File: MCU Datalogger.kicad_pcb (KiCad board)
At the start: 2 copper layers, 32 parts, among them J1 Conn_01x04_Pin, J2 Conn_01x04_Pin, J3 Conn_01x09_Pin, J4 Conn_02x03_Odd_Even, U1 24LC1025, U2 24LC1025, U3 ATMEGA328P-AU, U4 DS1337S_, Y1 32.768kHz, Y2 16KHz

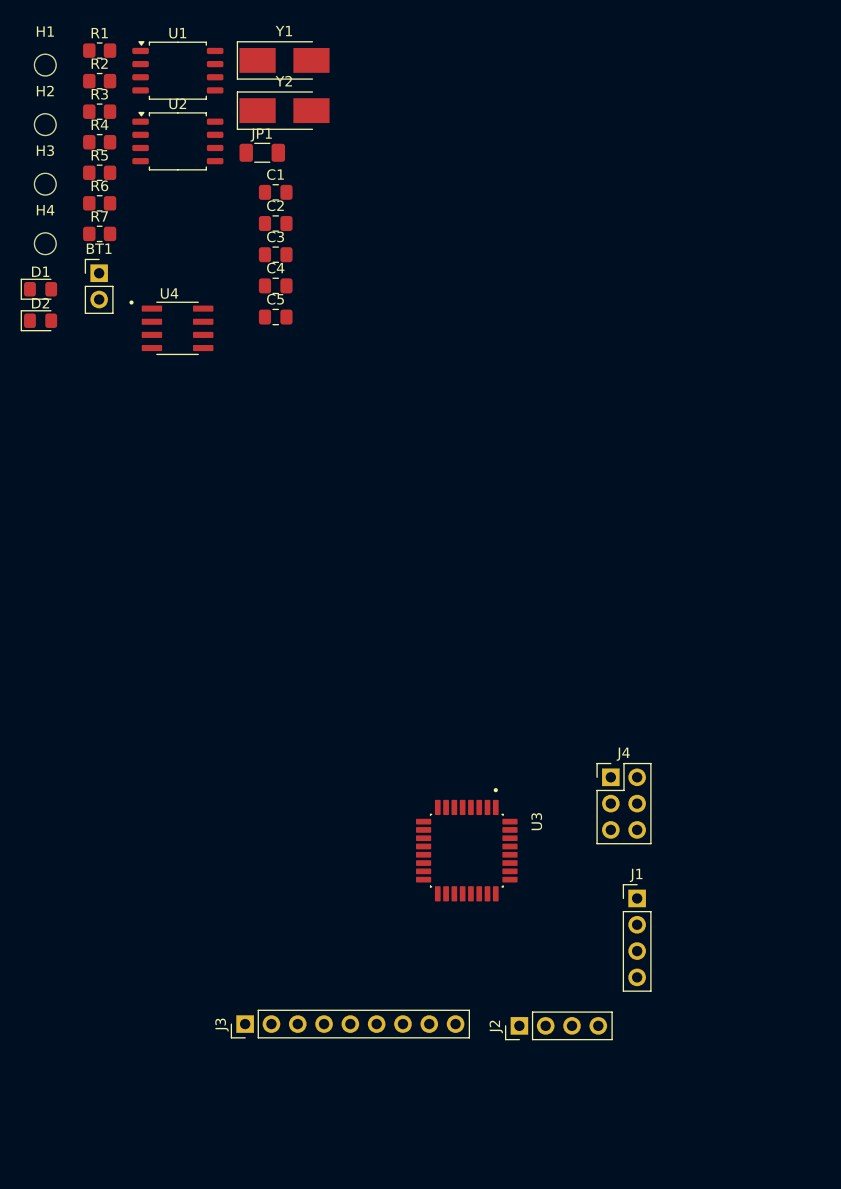
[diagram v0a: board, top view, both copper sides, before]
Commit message: finished the layout of the 4 layer PCB, still needs to finish silkscreen layer and review for any bugs
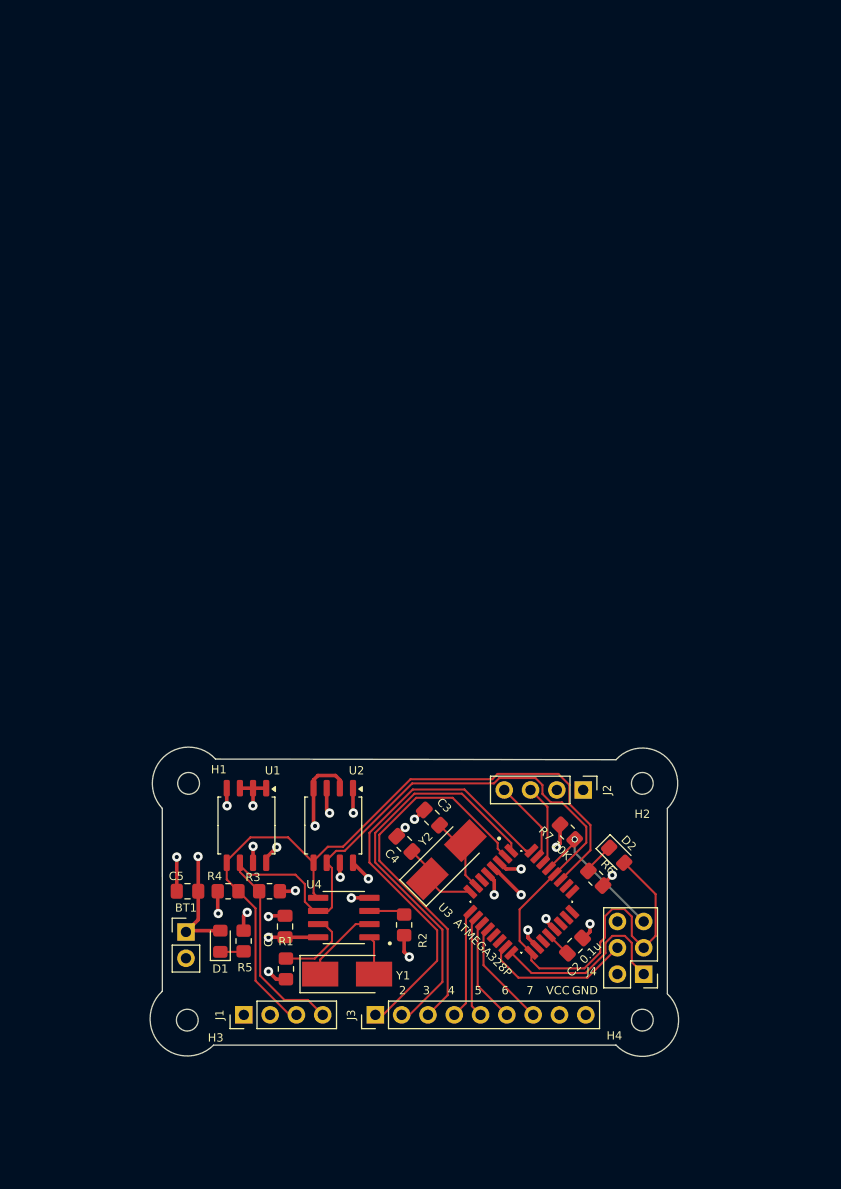
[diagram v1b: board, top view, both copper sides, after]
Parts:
- removed JP1: Jumper_2_Bridged, Resistor_SMD:R_1206_3216Metric_Pad1.30x1.75mm_HandSolder
- U3: value ATMEGA328P-AU -> ATMEGA328P
- moved H4 94.6 mm to (143.0, 115.7)
- moved R1 90.5 mm to (108.6, 110.8), turned to 90 degrees
- moved Y1 88.4 mm to (114.5, 111.3)
- moved R2 86.6 mm to (120.0, 106.5), turned to 90 degrees
- moved H2 85.9 mm to (143.0, 92.8)
- moved H3 81.9 mm to (99.1, 115.7)
- moved R6 80.9 mm to (138.5, 102.0), turned to 135 degrees
- moved R3 77.0 mm to (107.0, 103.2), turned to 180 degrees
- moved D2 75.9 mm to (140.5, 99.8), turned to -45 degrees
- moved C2 75.5 mm to (136.5, 108.5), turned to 45 degrees
- moved R5 75.5 mm to (104.5, 108.1), turned to 90 degrees
- moved Y2 74.0 mm to (124.1, 100.2), turned to 45 degrees
- moved R4 73.4 mm to (103.0, 103.2), turned to 180 degrees
- moved R7 73.3 mm to (135.8, 97.5), turned to 135 degrees
- moved U1 73.2 mm to (104.8, 96.9), turned to -90 degrees
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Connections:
- U3 pad 29: /RESET(JMP) -> /RESET
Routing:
- net /SCK: track 0.00 -> 110.9 mm
- net /SDA: track 0.00 -> 72.0 mm
- net /Vcc: track 0.00 -> 45.2 mm, vias 0 -> 14
- net /D2: track 0.00 -> 43.0 mm
- net /D3: track 0.00 -> 39.8 mm
- net /D4: track 0.00 -> 37.3 mm
- net GND: track 0.00 -> 32.8 mm, vias 0 -> 15
- net /MISO: track 0.00 -> 18.3 mm
- net /MOSI: track 0.00 -> 14.6 mm
- net /RESET: track 0.00 -> 14.5 mm, vias 0 -> 1
- net /D5: track 0.00 -> 10.6 mm
- net /D8: track 0.00 -> 10.4 mm
- net /D7: track 0.00 -> 10.2 mm
- net /D6: track 0.00 -> 9.91 mm
- net /TX: track 0.00 -> 8.10 mm
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- added copper zone on In2.Cu, net /Vcc
- added copper zone on In1.Cu, net GND
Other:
- board outline added: 51 x 29.9 mm
- copper layers 2 -> 4
- board text added: "2"
- board text added: "3"
- board text added: "4"
- board text added: "5"
- board text added: "6"
- board text added: "7"
- board text added: "GND"
- board text added: "VCC"

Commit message: finished the development of the 4 layer PCB, next step is to do a review on the design
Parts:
- moved R2 16.6 mm to (103.8, 103.2), turned to 0 degrees
- moved C1 11.9 mm to (119.7, 110.5), turned to 0 degrees
- moved R1 11.7 mm to (119.8, 107.2), turned to 180 degrees
- moved Y1 7.21 mm to (108.5, 107.2), turned to 90 degrees
- moved R3 6.73 mm to (109.5, 97.0), turned to -90 degrees
- moved R4 4.45 mm to (100.2, 99.8)
- moved R6 4.04 mm to (140.0, 98.2), turned to 90 degrees
- moved D2 3.12 mm to (143.2, 98.2), turned to -90 degrees
- moved J4 1.71 mm to (143.1, 109.5)
- moved C3 1.24 mm to (121.5, 96.5)
- moved U2 1.08 mm to (113.8, 96.0)
- moved C5 1.00 mm to (99.0, 104.2)
- moved U1 0.81 mm to (105.2, 96.2)
- moved U4 0.61 mm to (114.8, 106.0), turned to -90 degrees
- moved Y2 0.46 mm to (124.0, 99.8)
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- renumbered BT1 to POWER
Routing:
- net /SDA: track 72.0 -> 86.1 mm
- net Net-(U4-~{INTA}): track 3.49 -> 13.2 mm
- net Net-(U4-X1): track 3.74 -> 10.7 mm
- net /MOSI: track 14.6 -> 19.2 mm
- net /Vcc: track 45.2 -> 41.6 mm, vias 14 -> 12
- net Net-(U4-SQW/~INT): track 7.69 -> 4.58 mm
- net /MISO: track 18.3 -> 21.4 mm
- net Net-(U4-X2): track 7.57 -> 10.0 mm
- net Net-(U3-PB6): track 7.92 -> 9.17 mm
- net /D4: track 37.3 -> 38.4 mm
- net /SCK: track 110.9 -> 111.9 mm, vias 0 -> 1
- net /D3: track 39.8 -> 40.5 mm
- net GND: track 32.8 -> 33.4 mm, vias 15 -> 14
- net /D2: track 43.0 -> 43.7 mm
- net Net-(U3-AREF): track 2.71 -> 2.15 mm
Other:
- board text added: "1"
- board text added: "CLOCK"
- board text added: "EEPROM"
- board text added: "I2C"
- board text added: "RX"
- board text added: "SCK"
- board text added: "SDA"
- board text added: "TX"
- board text added: "UART"

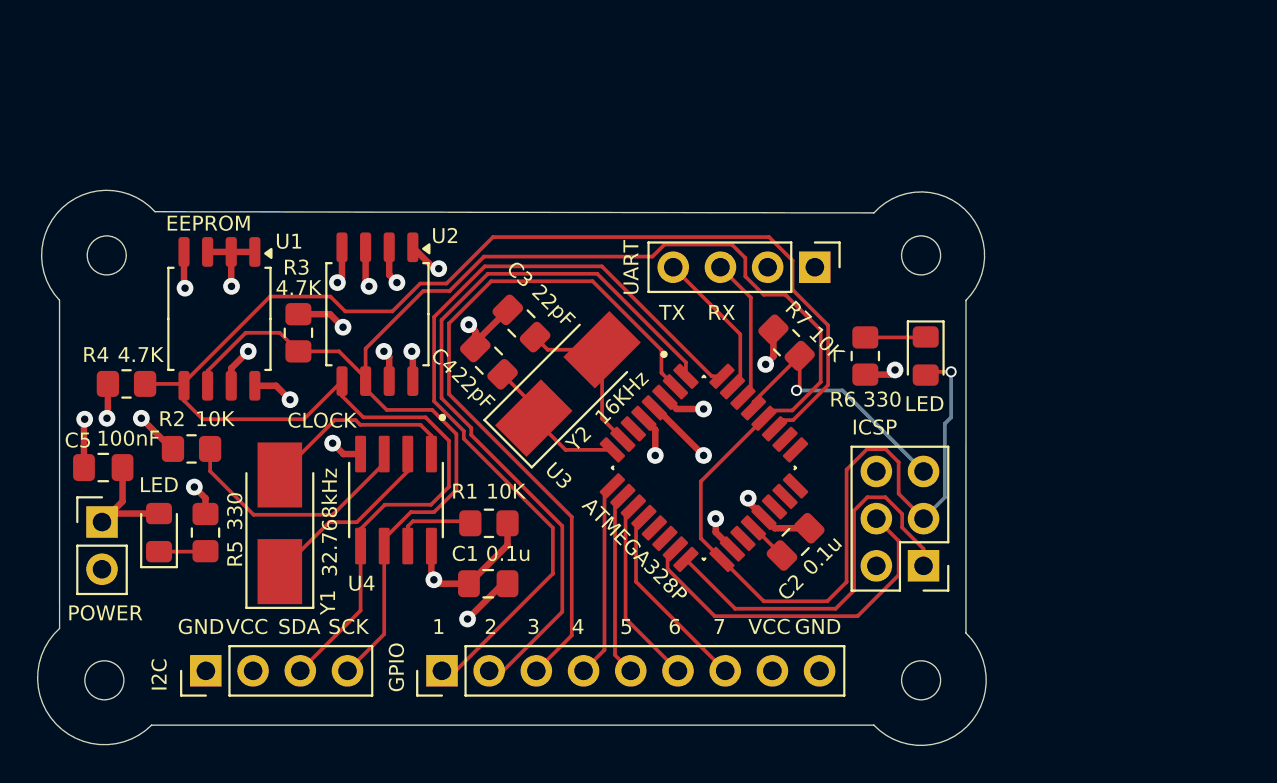
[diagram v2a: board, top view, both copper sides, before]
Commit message: started routing layout
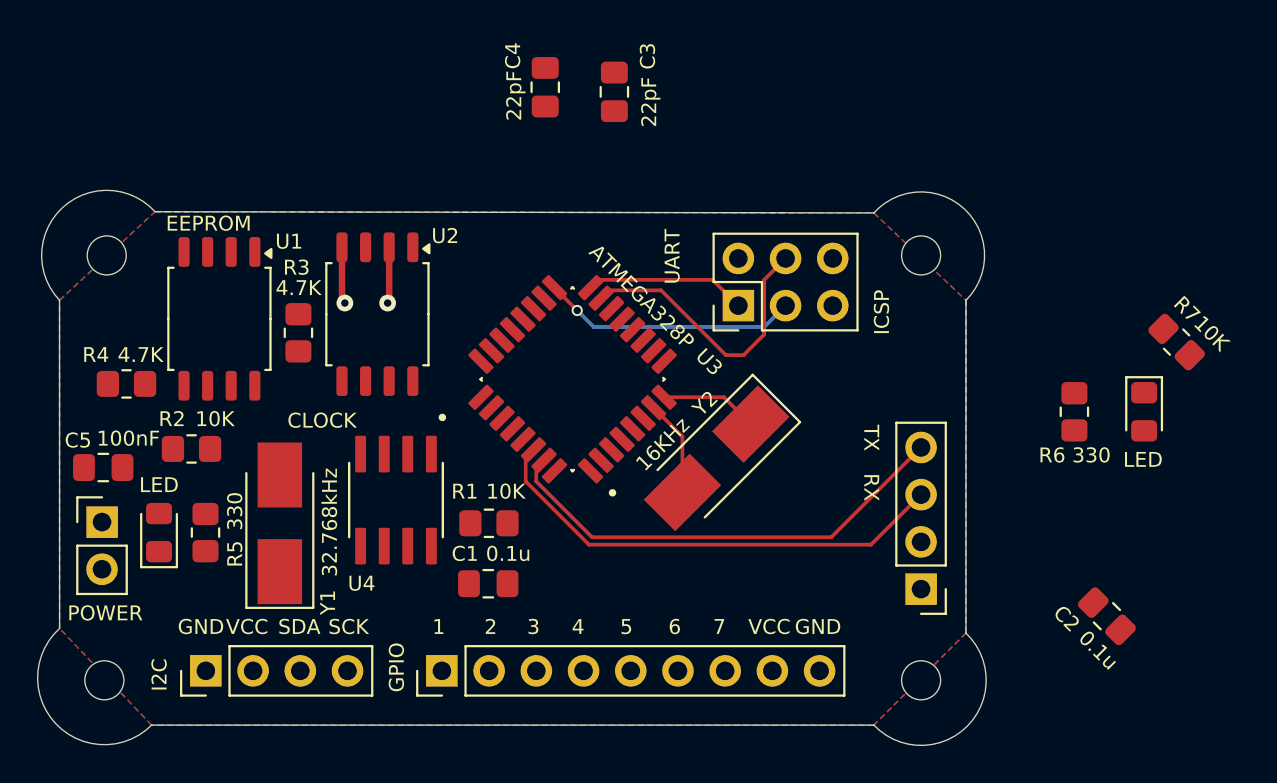
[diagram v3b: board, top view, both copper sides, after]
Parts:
- moved R7 21.0 mm to (156.8, 97.5)
- moved J2 18.2 mm to (143.0, 110.8), turned to 180 degrees
- moved C2 17.2 mm to (153.0, 112.2), turned to -45 degrees
- moved J4 17.2 mm to (133.2, 95.5), turned to 90 degrees
- moved C4 15.0 mm to (122.8, 83.8), turned to 90 degrees
- moved C3 13.4 mm to (126.5, 84.0), turned to -90 degrees
- moved D2 12.1 mm to (155.0, 101.2)
- moved R6 11.6 mm to (151.2, 101.2)
- moved Y2 8.94 mm to (132.0, 103.8), turned to -135 degrees
- moved U3 8.53 mm to (124.2, 99.5), turned to 135 degrees
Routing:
- net /SCK: track 111.9 -> 13.8 mm
- net /SDA: track 86.1 -> 0.00 mm
- net /D2: track 43.7 -> 0.00 mm
- net /Vcc: track 41.6 -> 0.00 mm, vias 12 -> 0
- net /D3: track 40.5 -> 0.00 mm
- net /D4: track 38.4 -> 0.00 mm
- net GND: track 33.4 -> 6.10 mm, vias 14 -> 2
- net /RX: track 7.85 -> 25.7 mm
- net /TX: track 8.10 -> 25.3 mm
- net /RESET: track 14.4 -> 0.00 mm, vias 1 -> 0
- net Net-(U4-~{INTA}): track 13.2 -> 0.00 mm
- net /MISO: track 21.4 -> 8.70 mm
- net Net-(U4-X1): track 10.7 -> 0.00 mm
- net /D5: track 10.6 -> 0.00 mm
- net /D8: track 10.4 -> 0.00 mm
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- added copper zone on F.Cu, net /Vcc
- added copper zone on B.Cu, net GND
- removed copper zone on In2.Cu, net /Vcc
- removed copper zone on In1.Cu, net GND
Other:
- copper layers 4 -> 2

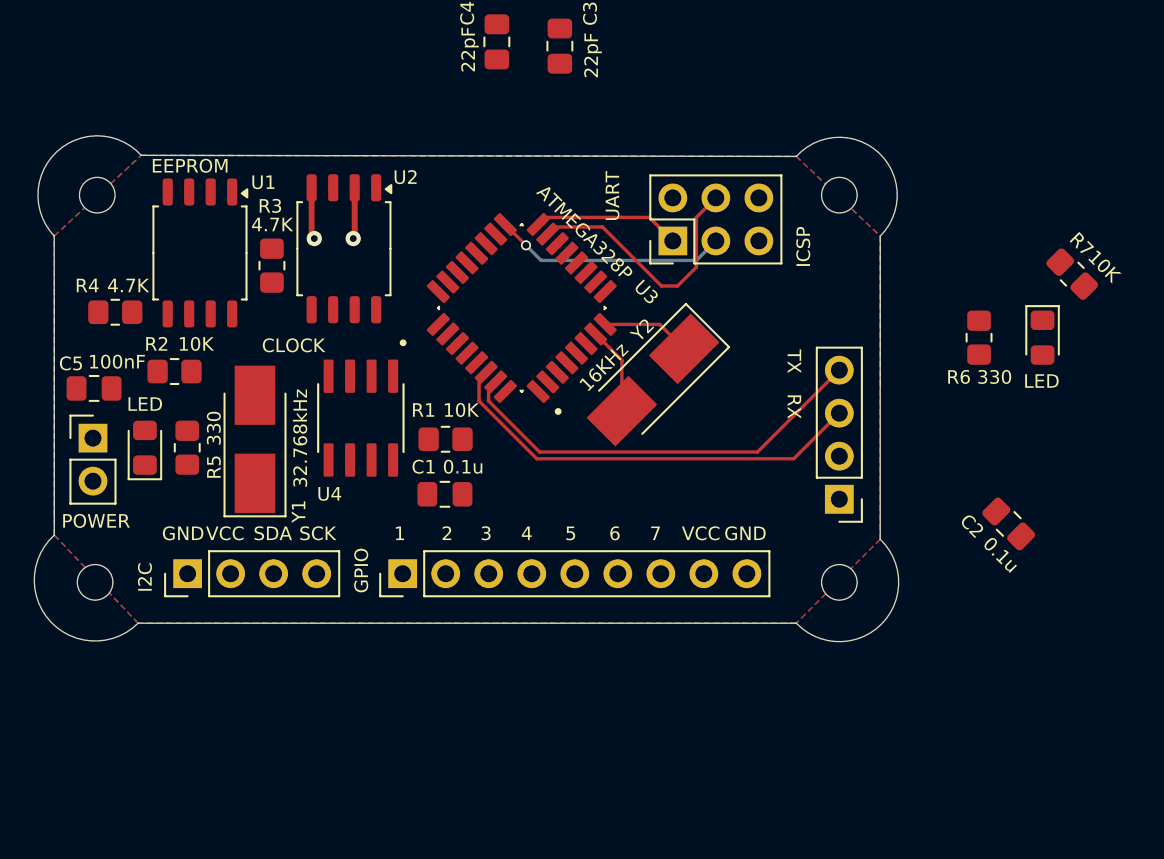
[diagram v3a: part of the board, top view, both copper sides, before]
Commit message: started routing layout
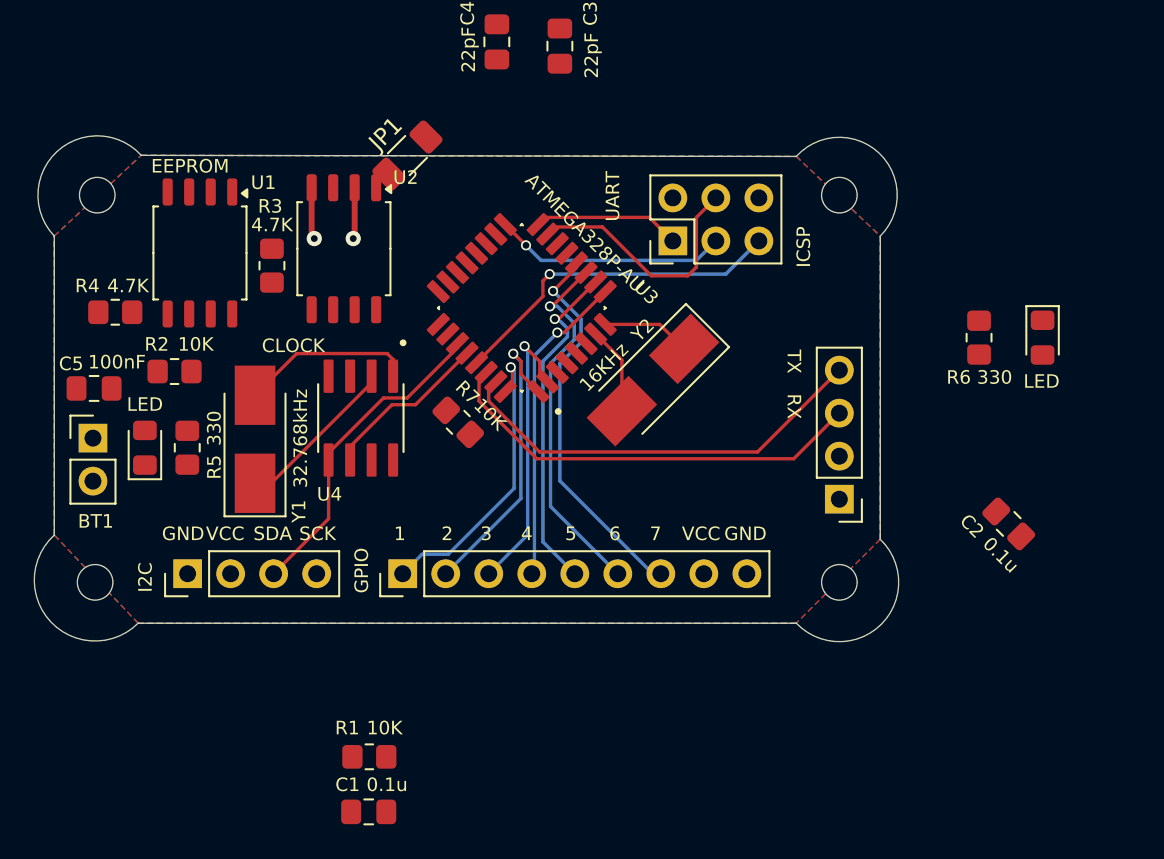
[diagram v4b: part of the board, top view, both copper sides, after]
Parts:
- added JP1: Jumper_2_Bridged, Resistor_SMD:R_1206_3216Metric_Pad1.30x1.75mm_HandSolder, F.Cu at (117.5, 90.5)
- U3: value ATMEGA328P -> ATMEGA328P-AU
- moved R7 37.3 mm to (120.5, 106.2)
- moved C1 19.3 mm to (115.2, 129.2)
- moved R1 19.3 mm to (115.2, 126.0)
- renumbered POWER to BT1
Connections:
- U1 pad 6: /SCK -> /SCL
- U2 pad 6: /SCK -> /SCL
- U3 pad 28: /SCK -> /SCL
- U4 pad 6: /SCK -> /SCL
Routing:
- net /D8: track 0.00 -> 22.9 mm, vias 0 -> 1
- net /D7: track 0.00 -> 21.8 mm, vias 0 -> 1
- net /RESET: track 0.00 -> 20.2 mm, vias 0 -> 1
- net /D6: track 0.00 -> 20.2 mm, vias 0 -> 1
- net /SDA: track 0.00 -> 18.9 mm
- net /D5: track 0.00 -> 18.7 mm, vias 0 -> 1
- net /D3: track 0.00 -> 17.9 mm, vias 0 -> 1
- net /D2: track 0.00 -> 17.5 mm, vias 0 -> 1
- net /D4: track 0.00 -> 17.1 mm, vias 0 -> 1
- net Net-(U4-X1): track 0.00 -> 10.3 mm
- net /SCL: track 0.00 -> 9.98 mm
- net Net-(U4-X2): track 0.00 -> 9.74 mm
